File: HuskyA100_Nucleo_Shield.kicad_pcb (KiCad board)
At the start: 2 copper layers, 58.4 x 99.1 mm, 20 parts, among them CN10 HEADER_17x2, CN7 HEADER_10x2, CN8 HEADER_8x2, CN9 HEADER_15x2, J1 Conn_01x03, J2 Conn_01x03, J3 Conn_01x04, J4 Conn_01x04

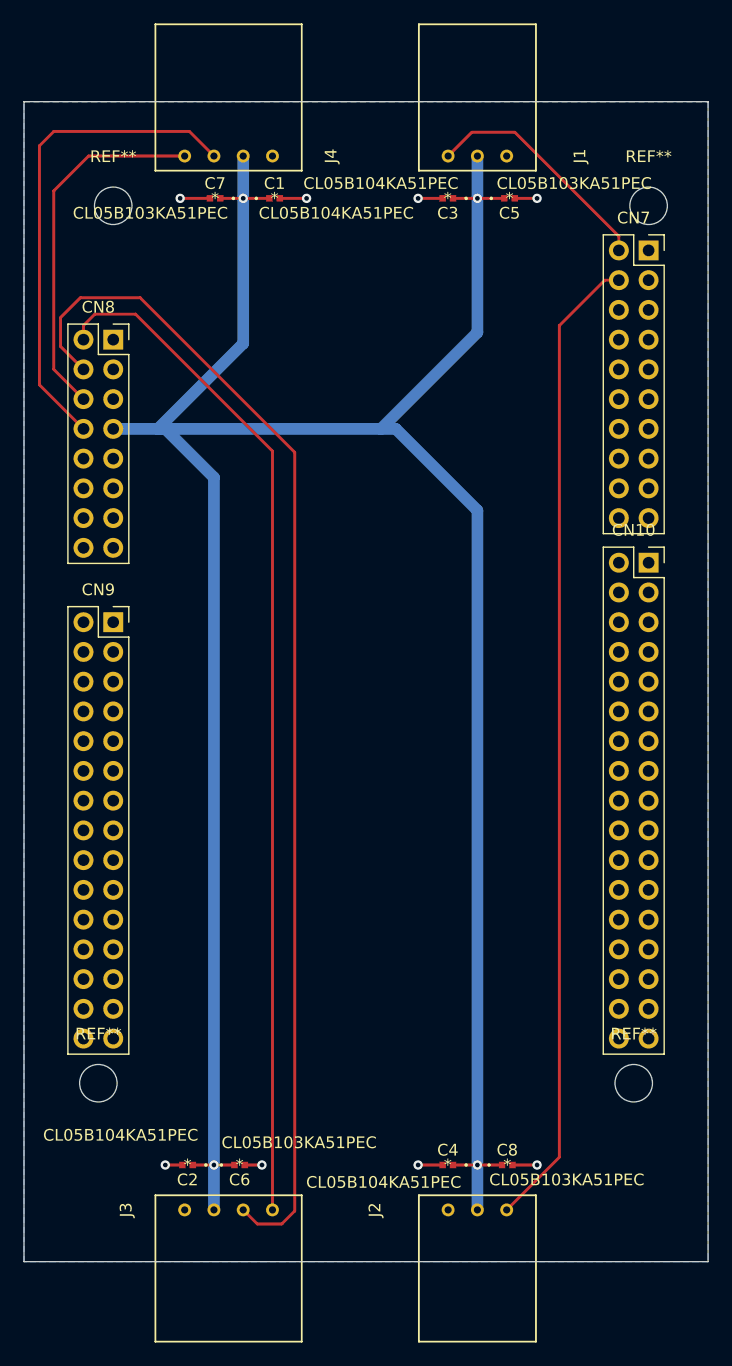
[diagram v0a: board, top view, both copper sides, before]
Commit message: rerouted the pins to be correct in the schematic + deleted old traces
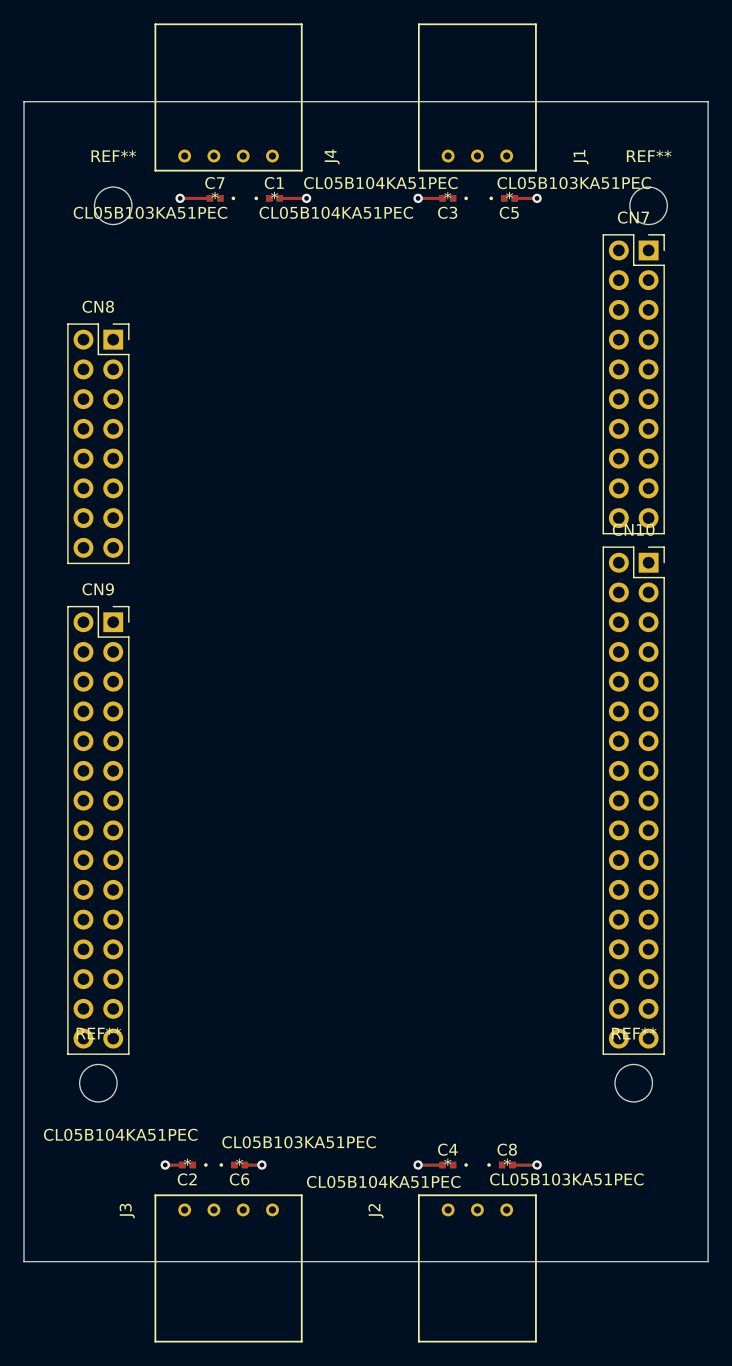
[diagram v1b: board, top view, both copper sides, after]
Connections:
- CN8 pad 10: Net-(CN8-Pad10) -> 5V
- CN8 pad 11: GND -> Net-(CN8-Pad11)
- CN8 pad 12: Net-(CN8-Pad12) -> GND
- CN8 pad 13: GND -> Net-(CN8-Pad13)
- CN8 pad 14: Net-(CN8-Pad14) -> GND
- CN8 pad 7: 3.3V -> Net-(CN8-Pad7)
- CN8 pad 8: Net-(CN8-Pad8) -> 3.3V
- CN8 pad 9: 5V -> Net-(CN8-Pad9)
- J1 pad 1: Net-(CN7-Pad2) -> Net-(CN7-Pad1)
- J2 pad 1: Net-(CN7-Pad4) -> Net-(CN7-Pad3)
- J3 pad 1: Net-(CN8-Pad2) -> Net-(CN8-Pad1)
- J3 pad 2: Net-(CN8-Pad4) -> Net-(CN8-Pad3)
- J4 pad 1: Net-(CN8-Pad6) -> Net-(CN8-Pad5)
- J4 pad 2: Net-(CN8-Pad8) -> Net-(CN8-Pad7)
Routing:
- net 3.3V: track 232.1 -> 0.00 mm, vias 4 -> 0
- net Net-(CN8-Pad4): track 101.6 -> 0.00 mm
- net Net-(CN8-Pad2): track 87.4 -> 0.00 mm
- net Net-(CN7-Pad4): track 84.1 -> 0.00 mm
- net Net-(CN8-Pad8): track 42.0 -> 0.00 mm
- net Net-(CN8-Pad6): track 31.2 -> 0.00 mm
- net Net-(CN7-Pad2): track 20.3 -> 0.00 mm
- removed copper zone on B.Cu, net GND

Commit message: fixed header connector spacing and mounting hole placement
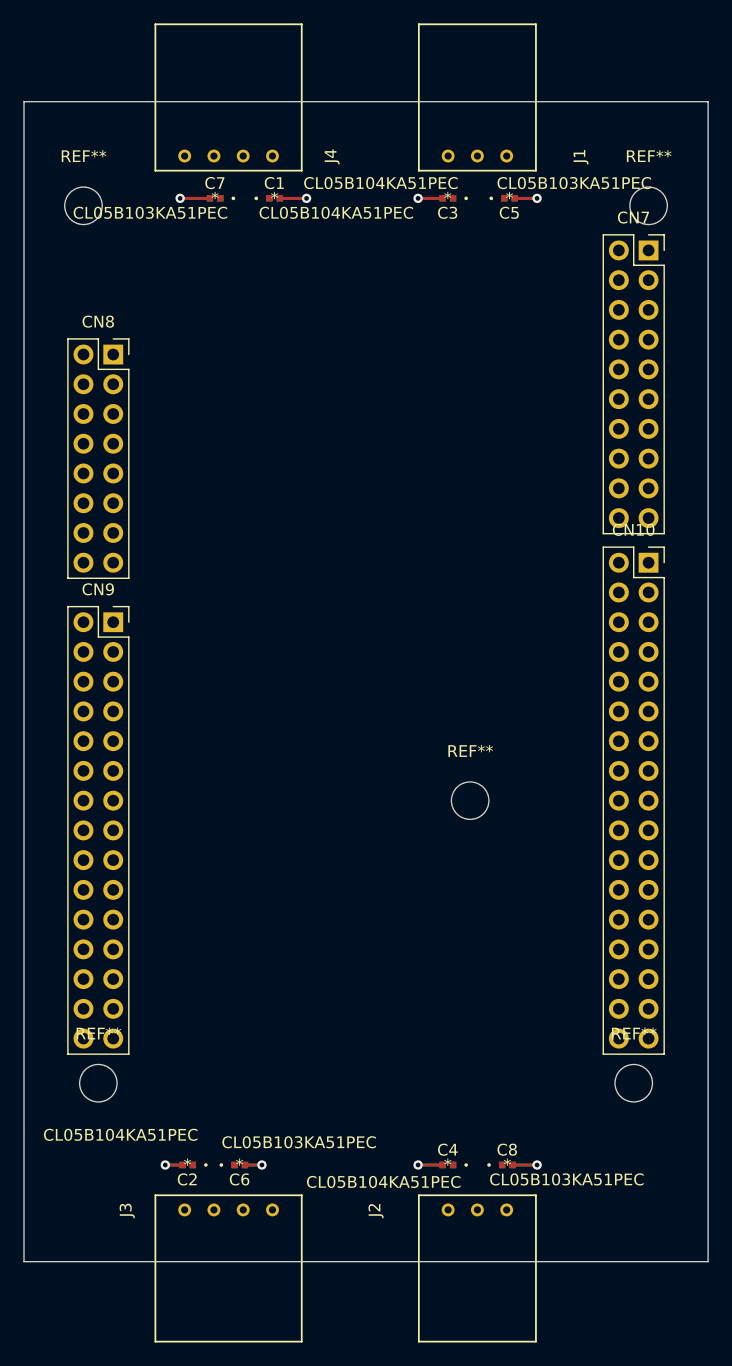
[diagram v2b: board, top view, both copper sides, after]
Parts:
- removed the REF** at (88.9, 31.8)
- added REF**: MountingHole_3.2mm_M3, MountingHole:MountingHole_3.2mm_M3, F.Cu at (86.4, 31.8)
- added REF**: MountingHole_3.2mm_M3, MountingHole:MountingHole_3.2mm_M3, F.Cu at (119.4, 82.5)
- moved CN8 1.27 mm to (88.9, 44.5)
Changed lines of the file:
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@@
     (tracks 16)
     (zones 0)
-    (modules 20)
+    (modules 21)
     (nets 99)
   )
@@
   )
   (module MountingHole:MountingHole_3.2mm_M3 (layer F.Cu)
-    (at 88.9 31.75)
+    (at 86.36 31.75)
     (descr "Mounting Hole 3.2mm, no annular, M3")
     (tags "mounting hole 3.2mm no annular m3")
@@
   )
   (module Connector_PinSocket_2.54mm:PinSocket_2x08_P2.54mm_Vertical (layer F.Cu)
-    (at 88.9 43.18)
+    (at 88.9 44.45)
     (descr "Through hole straight socket strip, 2x08, 2.54mm pitch, double cols (from Kicad 4.0.7), script generated")
     (tags "Through hole socket strip THT 2x08 2.54mm double row")
@@
       (net 9 "Net-(CN7-Pad3)"))
   )
+  (module MountingHole:MountingHole_3.2mm_M3 locked (layer F.Cu)
+    (at 119.38 82.55)
+    (descr "Mounting Hole 3.2mm, no annular, M3")
+    (tags "mounting hole 3.2mm no annular m3")
+    (attr virtual)
+    (fp_text reference REF** (at 0 -4.2) (layer F.SilkS)
+      (effects (font (size 1 1) (thickness 0.15)))
+    )
+    (fp_text value MountingHole_3.2mm_M3 (at 0 4.2) (layer F.Fab)
+      (effects (font (size 1 1) (thickness 0.15)))
+    )
+    (fp_circle (center 0 0) (end 3.45 0) (layer F.CrtYd) (width 0.05))
+    (fp_circle (center 0 0) (end 3.2 0) (layer Cmts.User) (width 0.15))
+    (fp_text user %R (at -5.08 0) (layer F.Fab)
+      (effects (font (size 1 1) (thickness 0.15)))
+    )
+    (pad 1 np_thru_hole circle (at 0 0) (size 3.2 3.2) (drill 3.2) (layers *.Cu *.Mask))
+  )
   (gr_line (start 139.7 121.92) (end 139.7 22.86) (layer Edge.Cuts) (width 0.1))
